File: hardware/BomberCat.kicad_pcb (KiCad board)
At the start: 2 copper layers, 65 x 38 mm, 82 parts, among them J1 Battery, J3 MAGSPOOF, P1 USB_C_Plug_USB2.0, Q1 DMG3415U-7, SW1 RESET, SW2 GPIO, U1 PN7150B0HN_C11002E, U2 RP2040, U3 MCP73831-3-OT, U4 AP2112K-3.3, U5 ESP32-WROOM-32D, U6 W25Q16JV, U7 TC4424, Y1 27.12Mhz, Y2 12Mhz

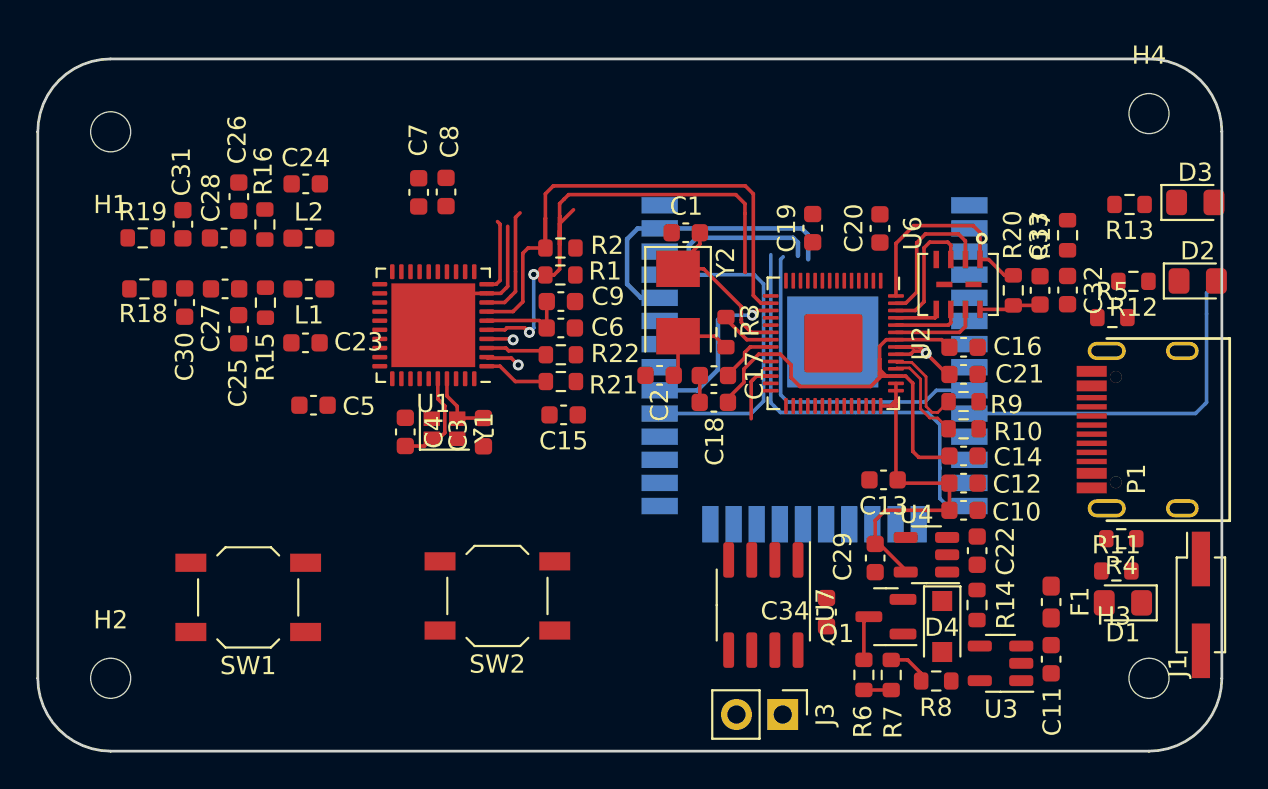
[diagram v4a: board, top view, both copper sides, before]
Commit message: add layout waiting for switch's
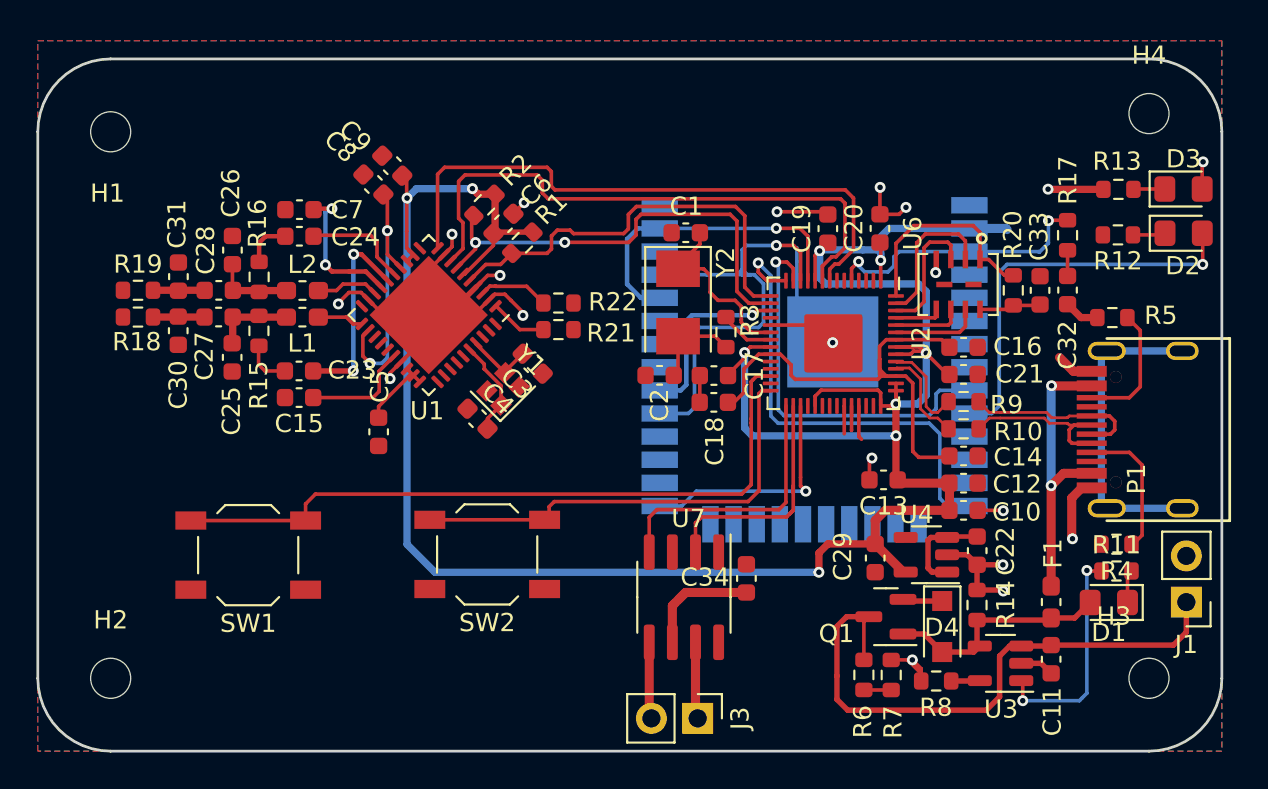
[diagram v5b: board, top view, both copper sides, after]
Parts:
- J1: footprint Connector_PinSocket_2.54mm:PinSocket_2x01_P2.54mm_Vertical_SMD -> Connector_PinHeader_2.54mm:PinHeader_1x02_P2.54mm_Vertical
- U1: value PN7150B0HN_C11002E -> PN7150B0HN_C11002E-PN7150B0HN_C11002E
- moved C15 14.6 mm to (106.3, 154.6)
- moved C9 11.9 mm to (111.5, 141.9), turned to 135 degrees
- moved C7 6.61 mm to (106.4, 144.3), turned to 180 degrees
- moved C6 6.53 mm to (117.6, 145.0), turned to 45 degrees
- moved R2 4.80 mm to (116.5, 144.0), turned to -135 degrees
- moved C34 4.78 mm to (130.9, 164.5)
- moved J3 4.67 mm to (128.2, 172.2)
- moved C3 4.63 mm to (119.2, 152.7), turned to -45 degrees
- moved U7 4.38 mm to (127.5, 165.6)
- moved C4 4.03 mm to (116.1, 155.8), turned to 135 degrees
- moved C8 4.01 mm to (110.4, 142.9), turned to 135 degrees
- moved Y1 3.88 mm to (117.5, 154.1), turned to 45 degrees
- moved C5 3.86 mm to (110.7, 156.5), turned to -90 degrees
- moved C26 2.96 mm to (102.7, 146.5)
- moved C24 2.90 mm to (106.4, 145.7)
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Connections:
- U2 pad 29: unconnected-(U2-Pad29) -> /IN_B
- U2 pad 30: unconnected-(U2-Pad30) -> /IN_A
- U2 pad 31: unconnected-(U2-Pad31) -> /ESP_GPIO0
- U2 pad 4: /ESP_GPIO0 -> unconnected-(U2-Pad4)
- U2 pad 6: /IN_A -> unconnected-(U2-Pad6)
- U2 pad 7: /IN_B -> unconnected-(U2-Pad7)
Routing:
- net +3V3: track 36.7 -> 162.2 mm, vias 1 -> 9
- net GND: track 15.5 -> 70.0 mm, vias 2 -> 18
- net /RST: track 3.24 -> 39.0 mm
- net +BATT: track 2.48 -> 32.6 mm
- net /VEN: track 4.10 -> 33.4 mm
- net /IRQ: track 6.25 -> 32.1 mm
- net /GPIO1: track 0.00 -> 25.0 mm
- net unconnected-(P1-PadS1): track 0.00 -> 17.2 mm
- net Net-(F1-Pad1): track 0.00 -> 15.7 mm, vias 0 -> 2
- net /ESP_RESET: track 0.00 -> 15.3 mm, vias 0 -> 2
- net /IN_B: track 0.00 -> 15.1 mm
- net Net-(C8-Pad1): track 0.00 -> 14.5 mm, vias 0 -> 2
- net /IN_A: track 0.00 -> 13.6 mm
- net /ESP_GPIO0: track 0.00 -> 13.2 mm, vias 0 -> 1
- net VBUS: track 0.00 -> 12.9 mm
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- added copper zone on B.Cu, net GND
- added copper zone on F.Cu, net GND

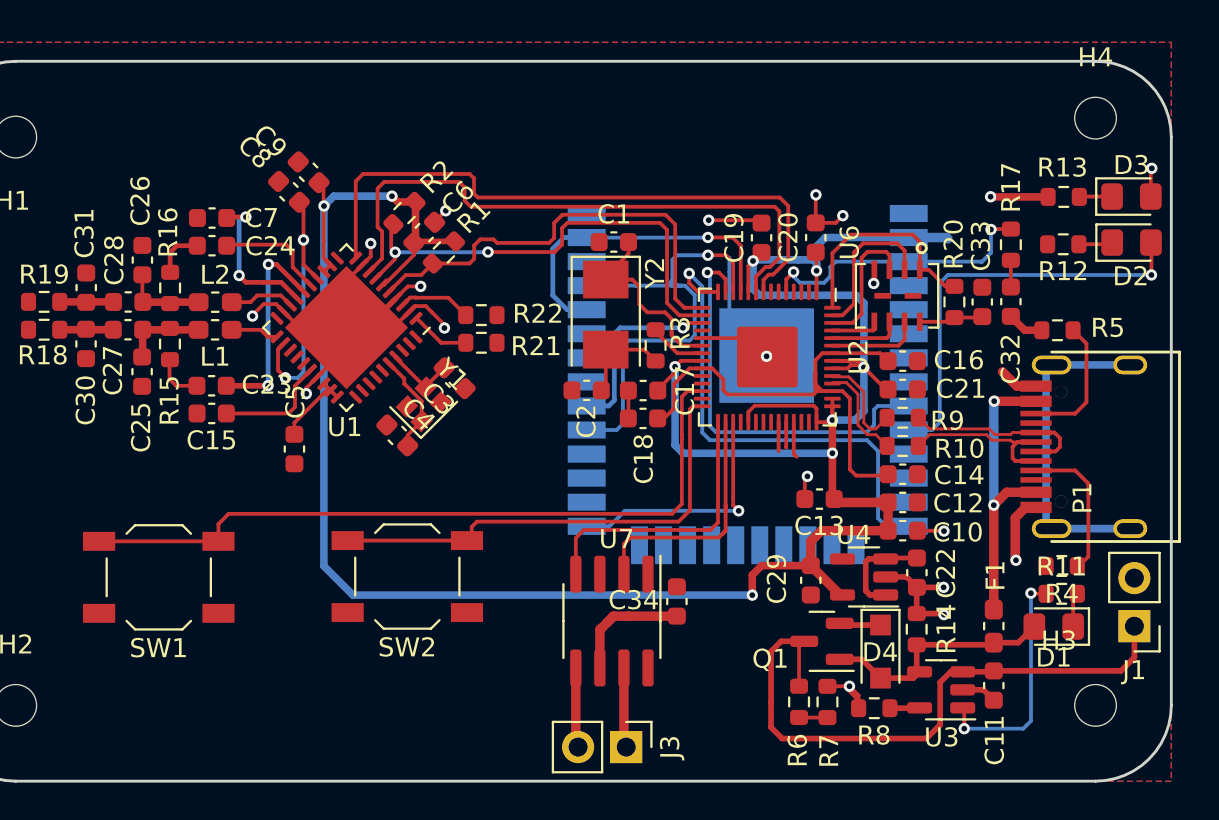
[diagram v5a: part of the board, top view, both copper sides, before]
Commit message: add labels
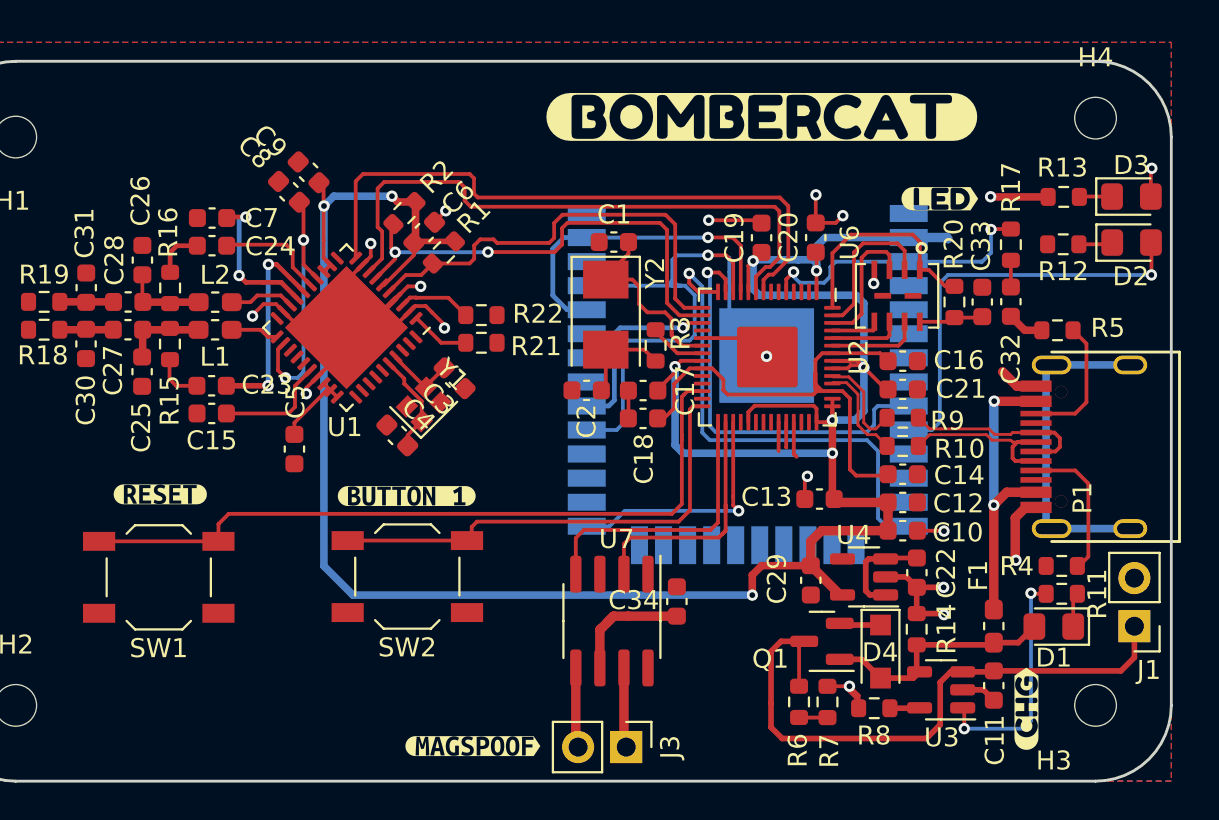
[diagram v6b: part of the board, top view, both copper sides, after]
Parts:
- added G***: LOGO, Aesthetics:electronic_cats_logo_8x6, B.Cu at (114.6, 157.7)
- added REF**: OSHW-Logo_7.5x8mm_SilkScreen, Symbol:OSHW-Logo_7.5x8mm_SilkScreen, B.Cu at (98.6, 158.0)
- added kibuzzard-62CC5774: G***, kibuzzard-62CC5774, F.Cu at (103.6, 158.9)
- added kibuzzard-62CC5787: G***, kibuzzard-62CC5787, F.Cu at (116.6, 158.9)
- added kibuzzard-62CC57AB: G***, kibuzzard-62CC57AB, F.Cu at (120.1, 172.2)
- added kibuzzard-62CC5892: G***, kibuzzard-62CC5892, F.Cu at (149.4, 170.2)
- added kibuzzard-62CC58B6: G***, kibuzzard-62CC58B6, F.Cu at (144.8, 143.3)
- added kibuzzard-62CC595D: G***, kibuzzard-62CC595D, B.Cu at (152.4, 145.7)
- added kibuzzard-62CC5B78: G***, kibuzzard-62CC5B78, F.Cu at (135.4, 138.9)
- added kibuzzard-62CC5B8F: G***, kibuzzard-62CC5B8F, B.Cu at (110.0, 147.1)
- added kibuzzard-62CC5BEF: G***, kibuzzard-62CC5BEF, B.Cu at (109.5, 149.6)

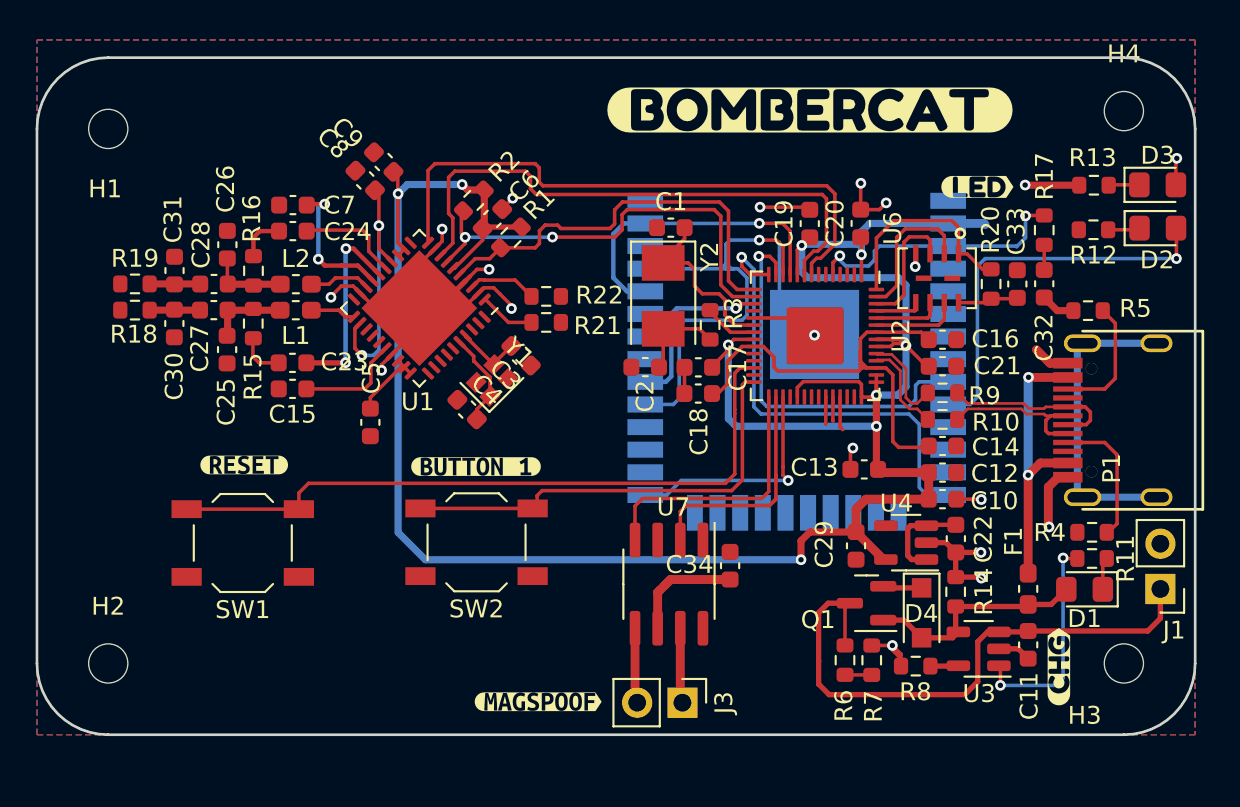
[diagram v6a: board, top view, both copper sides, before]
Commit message: layout update 0 unconnected added switchs
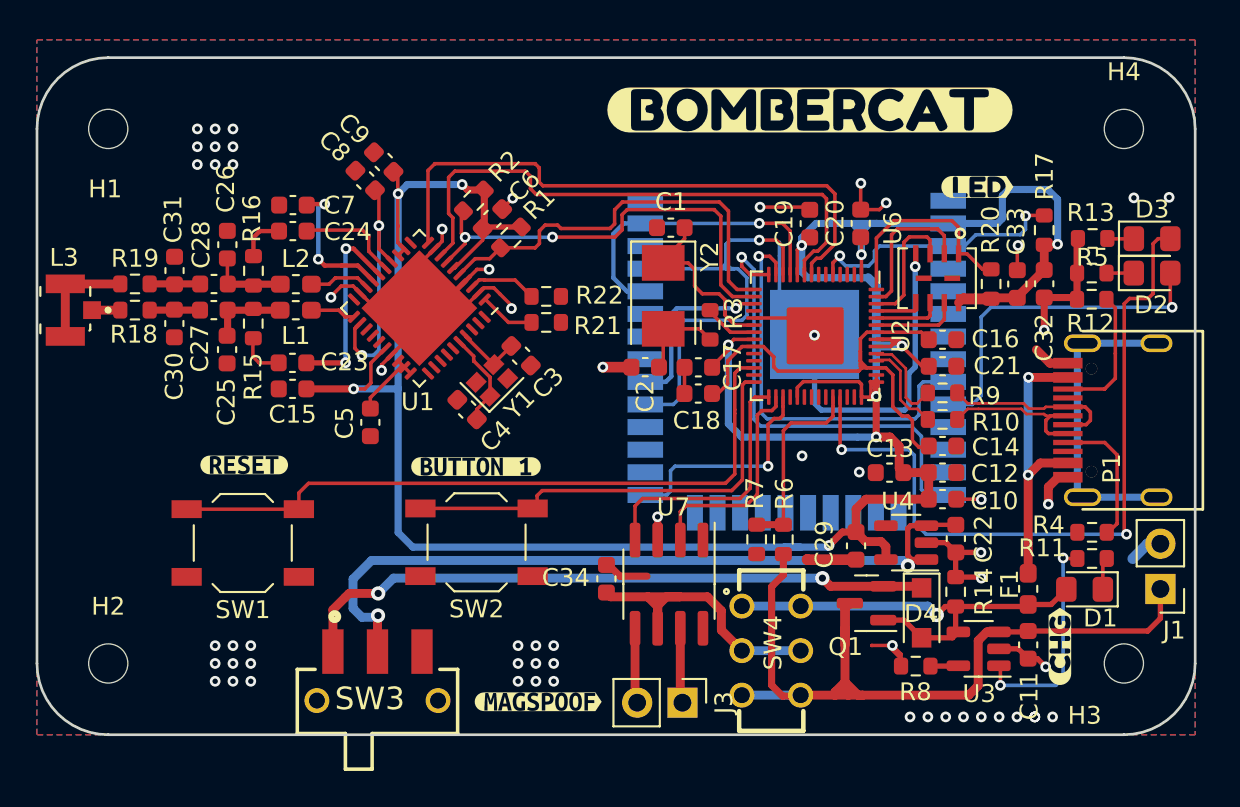
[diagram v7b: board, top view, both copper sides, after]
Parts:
- added L3: L, Connectors:MOLEX_1661, F.Cu at (93.6, 150.2)
- added SW3: ON, BomberCat:JS102011SAQN, F.Cu at (111.1, 170.3)
- added SW4: SOURCE MAG, BomberCat:JS202011CQN, F.Cu at (133.2, 169.3)
- moved R7 9.37 mm to (132.4, 163.0), turned to -90 degrees
- moved R6 7.61 mm to (133.9, 163.0), turned to 90 degrees
- moved C34 6.98 mm to (124.0, 165.2)
- moved D3 3.04 mm to (154.6, 146.2)
- moved R13 2.99 mm to (151.2, 146.2)
- moved D2 2.54 mm to (154.6, 148.1)
- moved R12 2.43 mm to (151.2, 148.1)
- moved C13 1.43 mm to (139.8, 159.3)
- moved kibuzzard-62CC5892 1.14 mm to (149.4, 169.0)
- moved H4 1.00 mm to (153.0, 140.0)
- moved R5 0.67 mm to (151.2, 149.6)
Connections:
- U2 pad 37: /LED1 -> unconnected-(U2-Pad37)
- U2 pad 39: unconnected-(U2-Pad39) -> /LED1
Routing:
- net GND: track 70.0 -> 116.9 mm, vias 18 -> 63
- net /LED1: track 3.04 -> 41.9 mm, vias 1 -> 2
- net Net-(C22-Pad1): track 5.45 -> 43.7 mm, vias 0 -> 2
- net Net-(D4-Pad1): track 2.19 -> 36.4 mm, vias 0 -> 2
- net unconnected-(P1-PadS1): track 17.2 -> 0.00 mm
- net +BATT: track 32.6 -> 48.6 mm
- net +3V3: track 162.2 -> 177.7 mm, vias 9 -> 11
- net VBUS: track 12.9 -> 25.3 mm, vias 0 -> 1
- net Net-(C34-Pad1): track 7.40 -> 17.6 mm
- net /B_ADC: track 2.83 -> 11.0 mm
- net Net-(L3-Pad2): track 0.00 -> 6.04 mm
- net /ESP_LED: track 22.2 -> 19.4 mm
- net unconnected-(U2-Pad39): track 1.89 -> 0.00 mm
- net Net-(L3-Pad1): track 0.00 -> 1.58 mm
- net /ACK_CTS: track 21.6 -> 23.1 mm
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
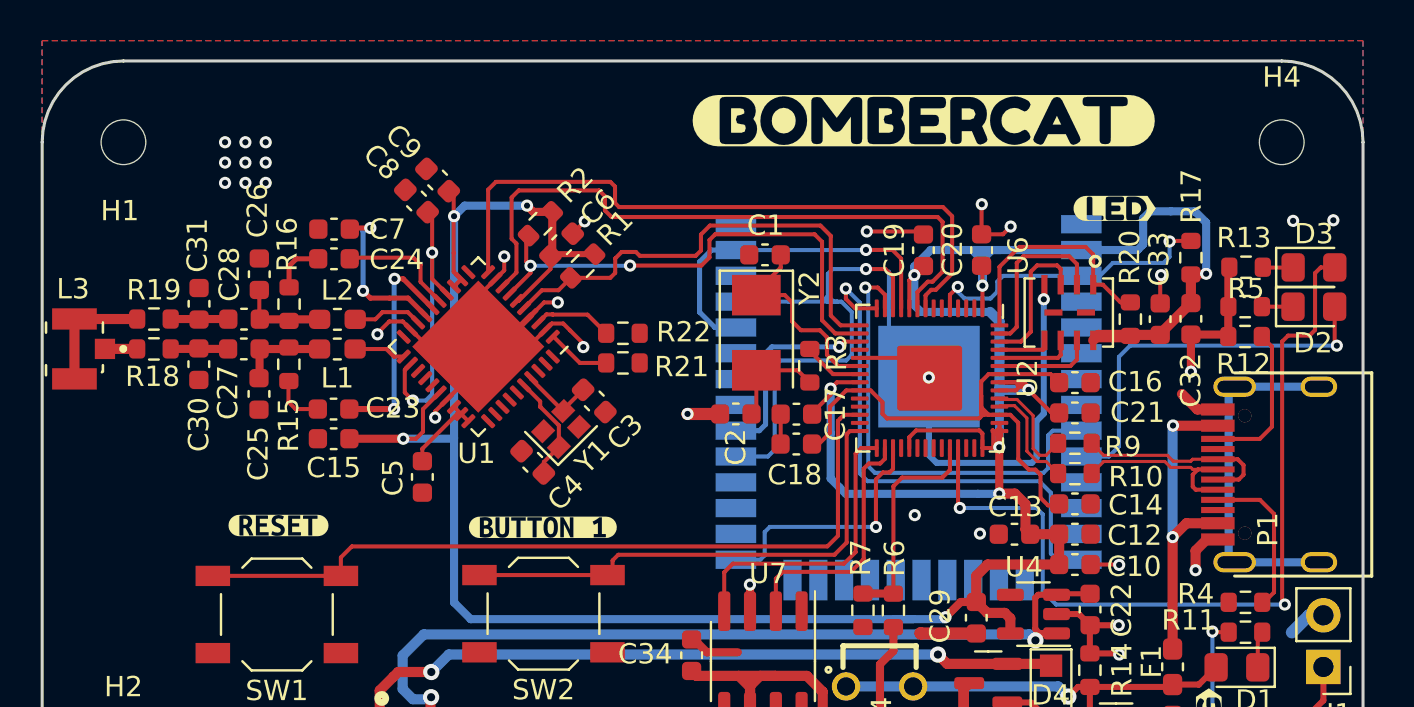
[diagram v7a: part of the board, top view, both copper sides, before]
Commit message: add logos for defcon edition
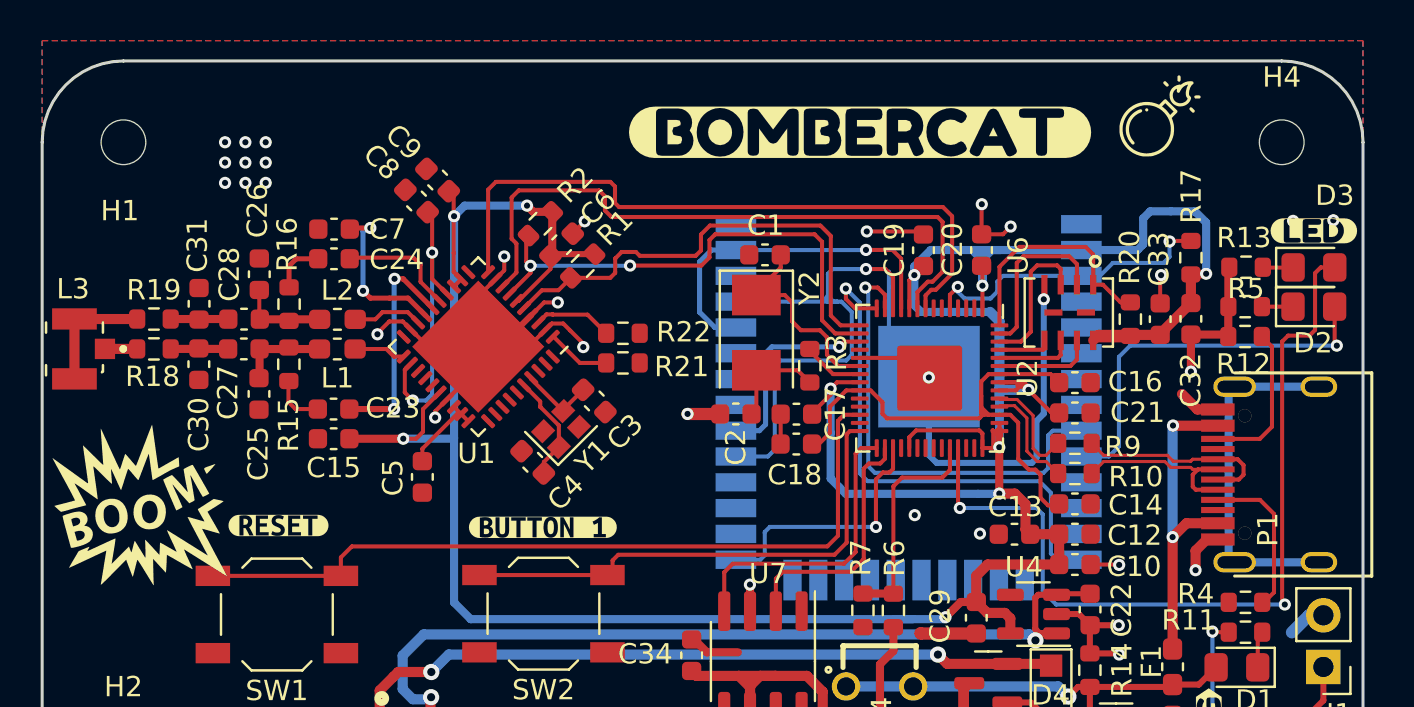
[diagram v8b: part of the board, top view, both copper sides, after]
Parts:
- removed kibuzzard-62CC58B6: G***, kibuzzard-62CC58B6
- added G***: LOGO, LOGO, F.Cu at (96.8, 157.8)
- added G***: LOGO, LOGO, F.Cu at (147.0, 138.7)
- added G***: LOGO, LOGO, B.Cu at (103.8, 152.4)
- added kibuzzard-62CC5B78: G***, kibuzzard-62CC5B78, B.Cu at (109.2, 142.8)
- added kibuzzard-62CC9912: G***, kibuzzard-62CC9912, B.Cu at (109.2, 146.9)
- added kibuzzard-62CC9A49: G***, kibuzzard-62CC9A49, F.Cu at (154.6, 144.4)
- moved G*** 5.82 mm to (117.0, 163.0)
- moved kibuzzard-62CC5BEF 5.30 mm to (112.9, 153.7)
- moved REF** 5.19 mm to (99.5, 163.1)
- moved kibuzzard-62CC5B78 3.18 mm to (132.2, 139.5)
- moved kibuzzard-62CC5B8F 1.96 mm to (109.7, 145.1)
